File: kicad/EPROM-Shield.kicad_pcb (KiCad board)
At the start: 2 copper layers, 61 x 54.6 mm, 23 parts, among them J1 D8-D13, J2 Conn_01x06, J3 D0-D7, J4 A0-A5, U1 74LS595, U2 74LS595, U3 28C256

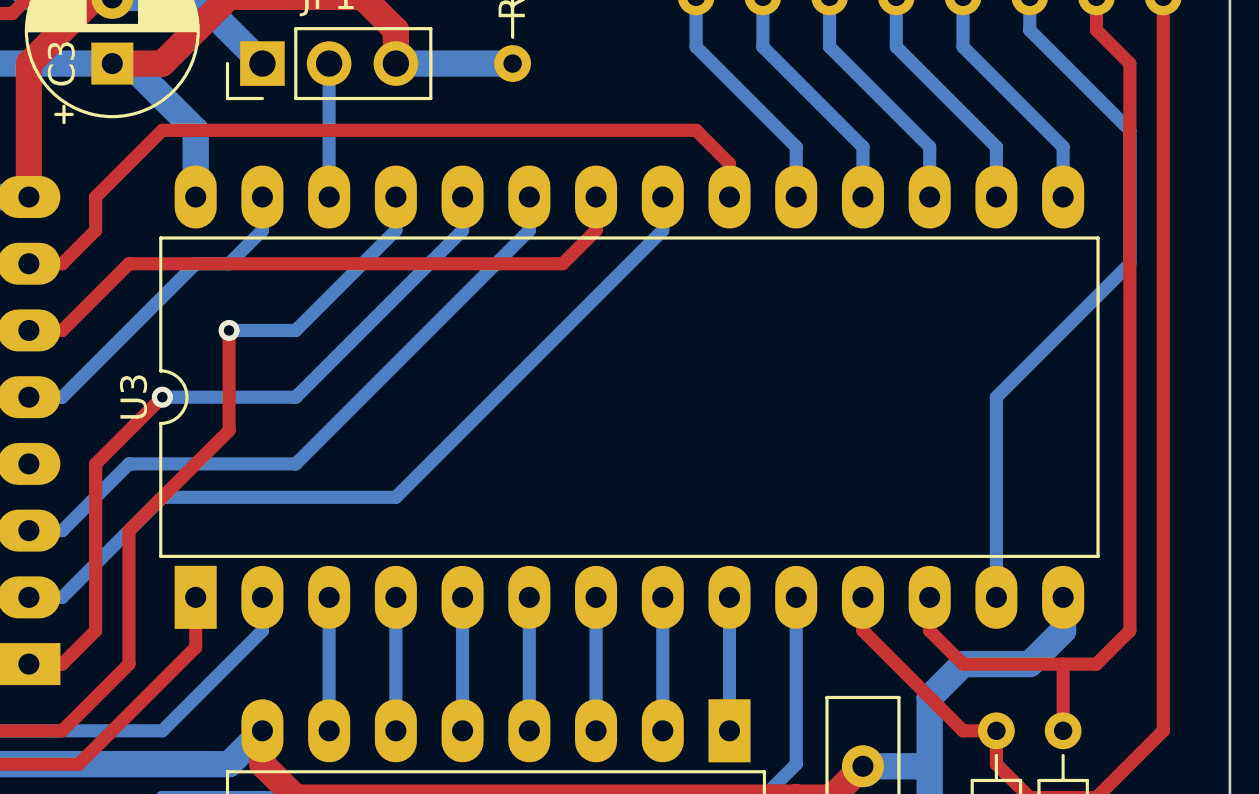
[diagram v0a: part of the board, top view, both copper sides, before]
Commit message: change footprint of EEPROM to one with socket
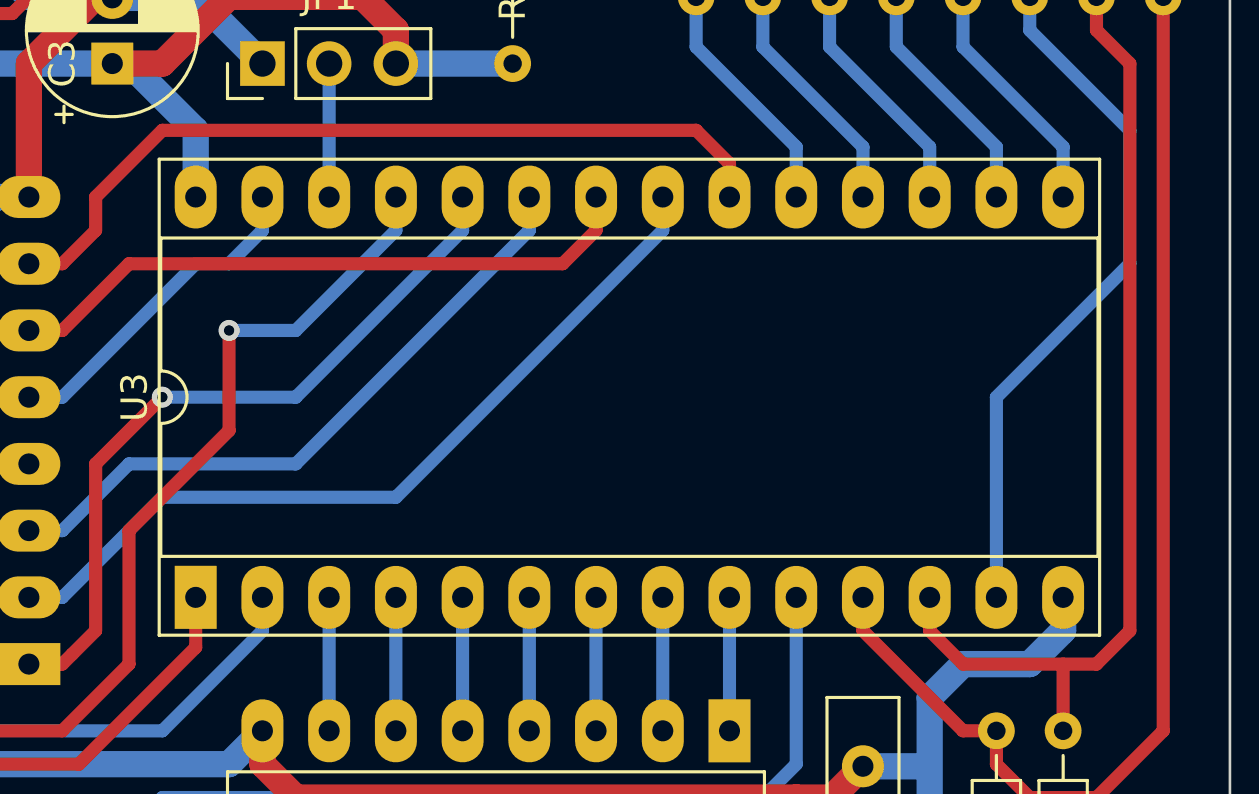
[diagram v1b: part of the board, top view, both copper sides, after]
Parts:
- U3: footprint Package_DIP:DIP-28_W15.24mm_LongPads -> Package_DIP:DIP-28_W15.24mm_Socket_LongPads
